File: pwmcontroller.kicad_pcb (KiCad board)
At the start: 2 copper layers, 35.1 x 44.5 mm, 19 parts, among them J1 CONN_01X04, J2 CONN_01X04, U1 WPMIx9200501S, U2 NE555

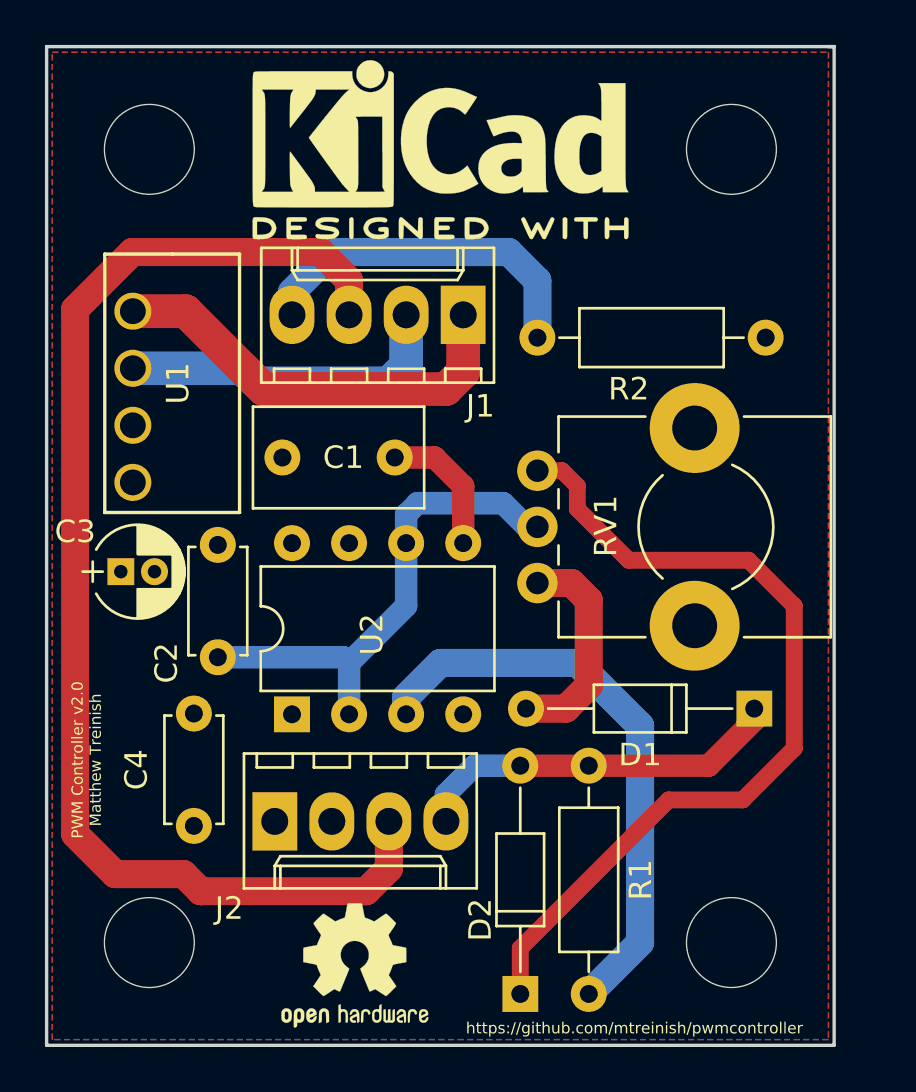
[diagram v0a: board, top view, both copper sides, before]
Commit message: Add fan header labels
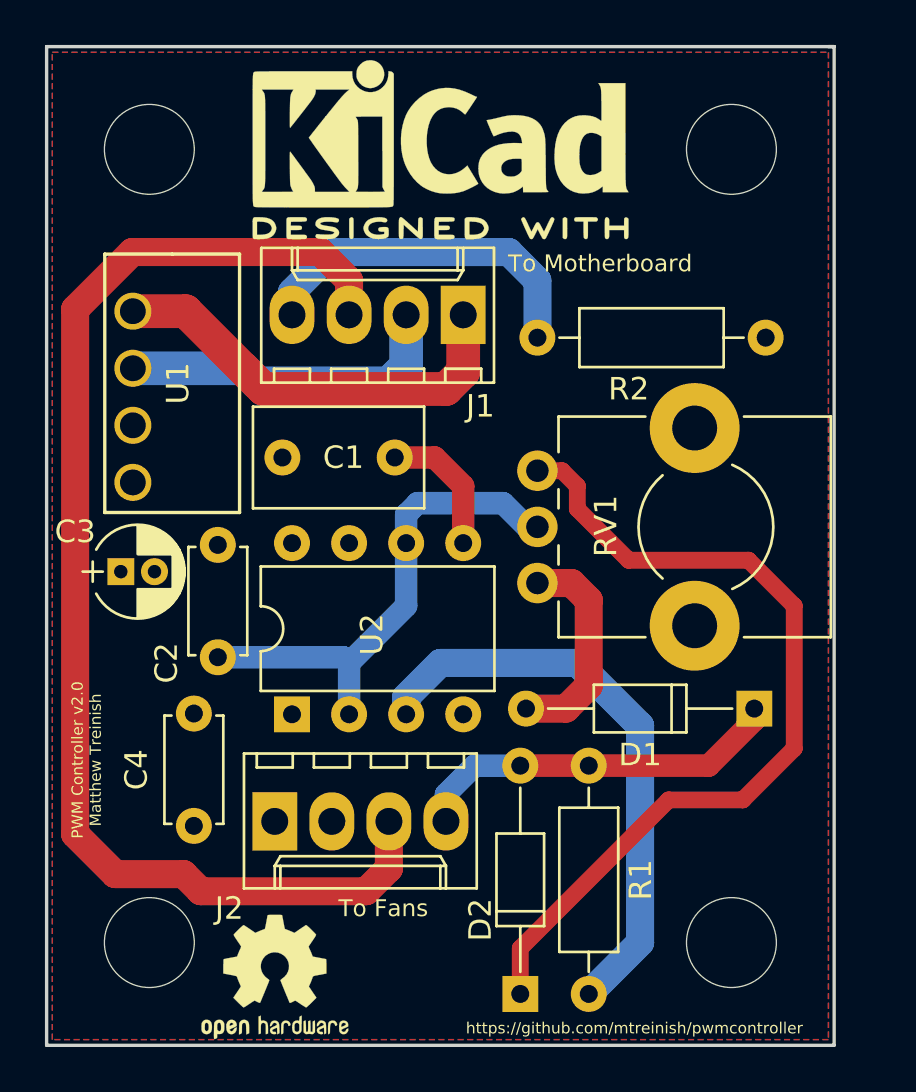
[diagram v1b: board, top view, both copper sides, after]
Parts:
- moved REF*** 3.59 mm to (149.6, 131.3)
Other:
- board text added: "To Fans"
- board text added: "To Motherboard"
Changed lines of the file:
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@@
     (area 139.370999 88.513 174.765001 135.869)
     (thickness 1.6)
-    (drawings 7)
+    (drawings 9)
     (tracks 68)
     (zones 0)
@@
   )
   (module Symbols:OSHW-Logo2_7.3x6mm_SilkScreen (layer F.Cu)
-    (at 153.162 130.81)
+    (at 149.606 131.318)
     (descr "Open Source Hardware Symbol")
     (tags "Logo Symbol OSHW")
@@
     )
   )
+  (gr_text "To Motherboard" (at 164.084 99.568) (layer F.SilkS)
+    (effects (font (size 0.75 0.75) (thickness 0.1875)))
+  )
+  (gr_text "To Fans" (at 154.432 128.27) (layer F.SilkS)
+    (effects (font (size 0.75 0.75) (thickness 0.1875)))
+  )
   (gr_text https://github.com/mtreinish/pwmcontroller (at 165.608 133.604) (layer F.SilkS)

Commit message: Add Schmitt Trigger Output Buffer
This commit adds a schmitt trigger output buffer to clean up the output
signal.
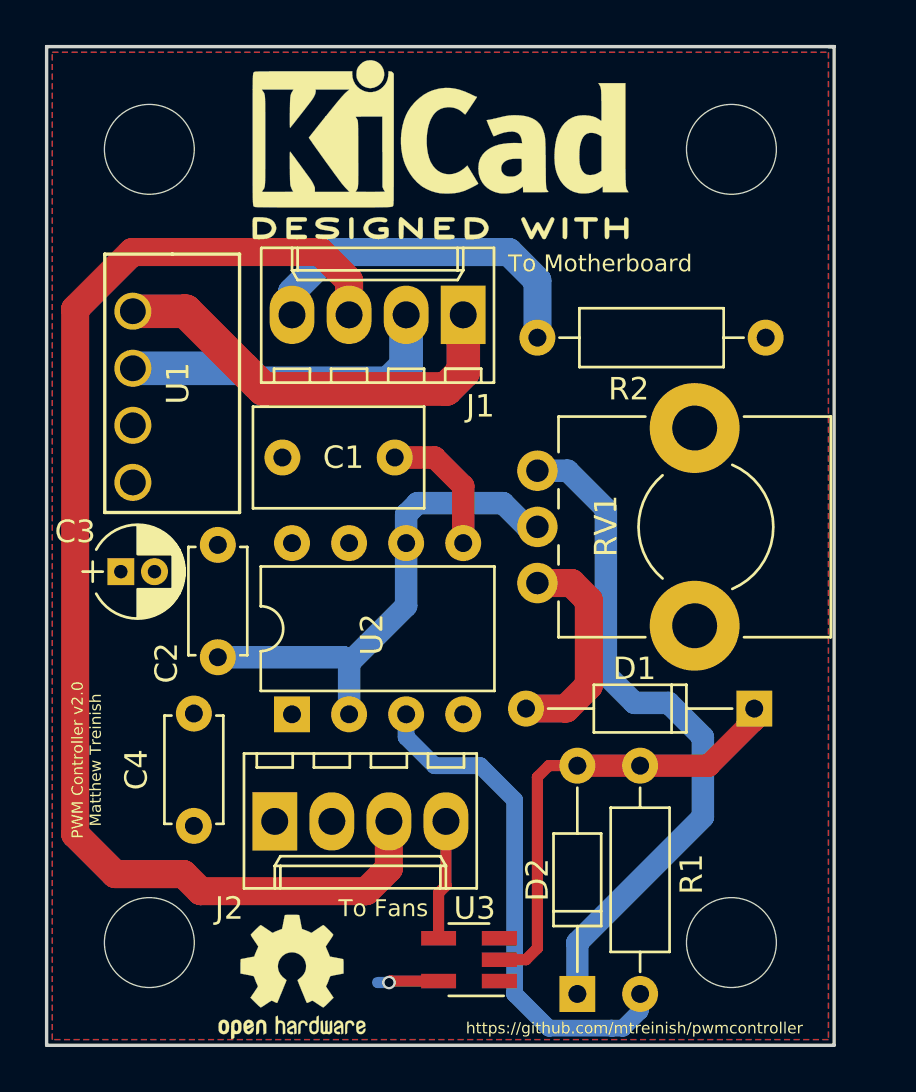
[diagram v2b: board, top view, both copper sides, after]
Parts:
- added U3: 74AHC1G14, TO_SOT_Packages_SMD:SOT-23-5_HandSoldering, F.Cu at (158.2, 130.6)
- moved D2 2.54 mm to (163.1, 132.1)
- moved R1 2.29 mm to (165.9, 121.9)
- moved REF*** 0.76 mm to (150.4, 131.3)
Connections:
- J2 pad 4: /PWM_OUT -> Net-(J2-Pad4)
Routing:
- net Net-(D2-Pad1): track 38.8 -> 30.3 mm
- net Net-(J2-Pad4): track 0.00 -> 5.34 mm
- net /PWM_OUT: track 16.8 -> 21.2 mm
- net Net-(R1-Pad2): track 25.8 -> 22.9 mm
- net VCC: track 0.00 -> 2.74 mm, vias 0 -> 1

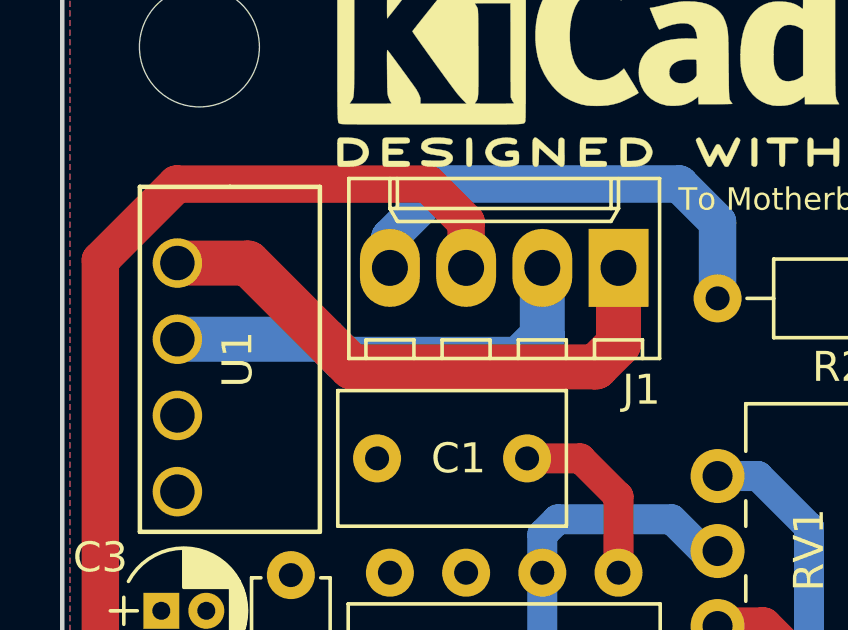
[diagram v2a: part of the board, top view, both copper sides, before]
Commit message: Fix floating output ground
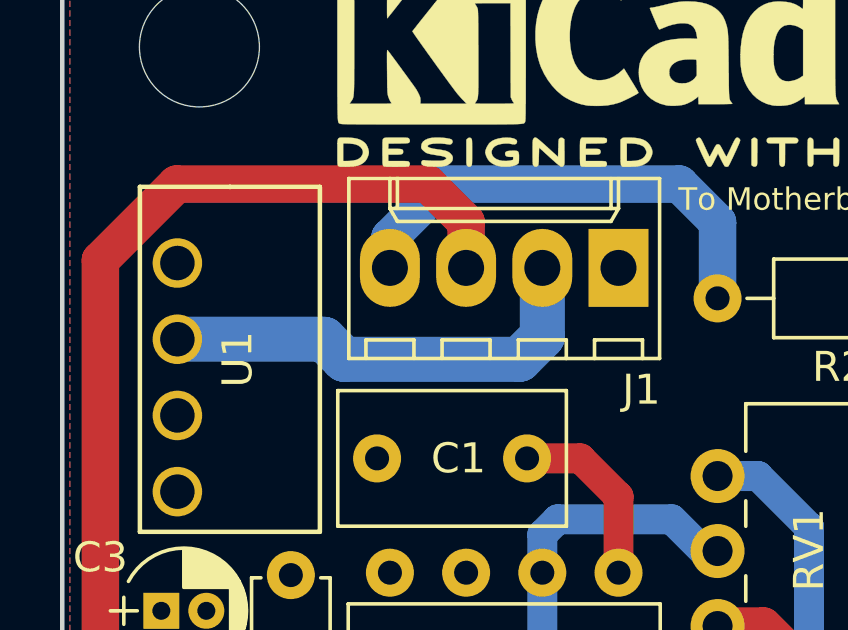
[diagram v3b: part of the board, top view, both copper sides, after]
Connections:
- J1 pad 1: GNDS -> GND
- U1 pad 1: GNDS -> GND
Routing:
- net GNDS: track 19.0 -> 0.00 mm

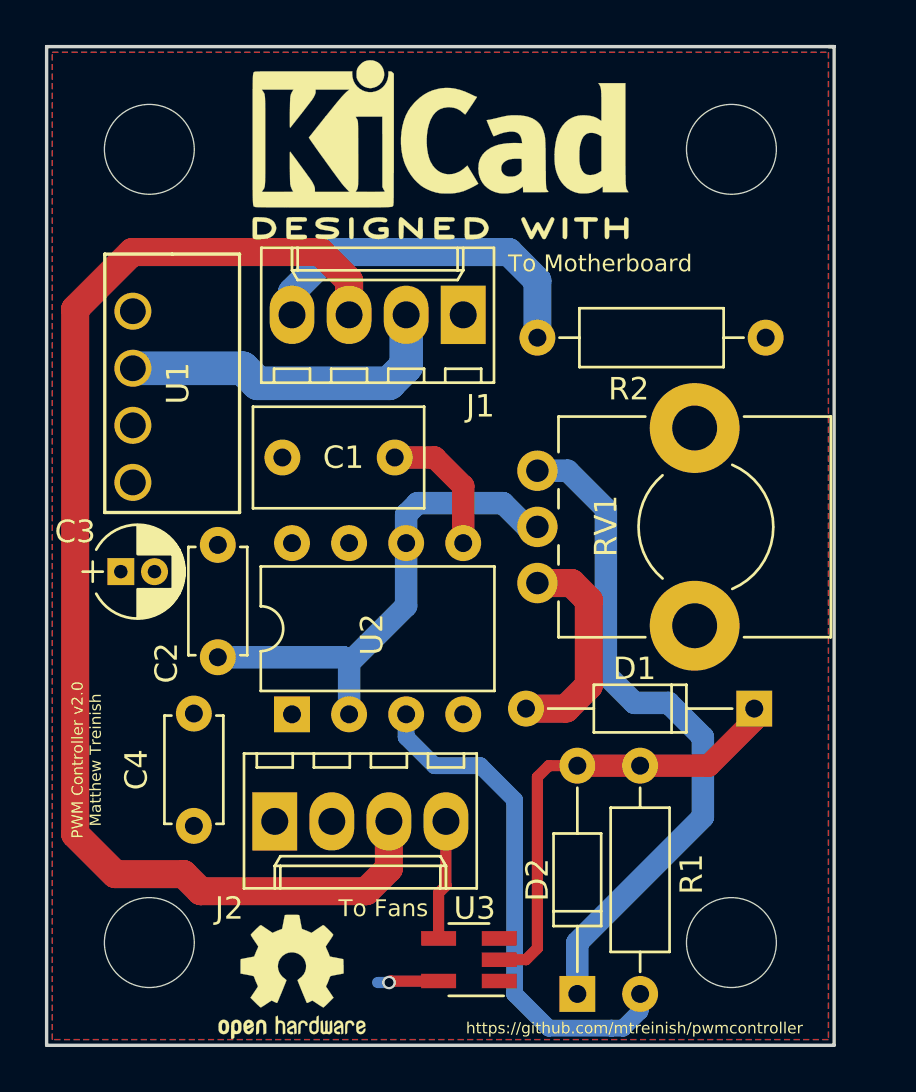
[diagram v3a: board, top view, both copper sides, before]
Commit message: Pivot to revision 3 of the design
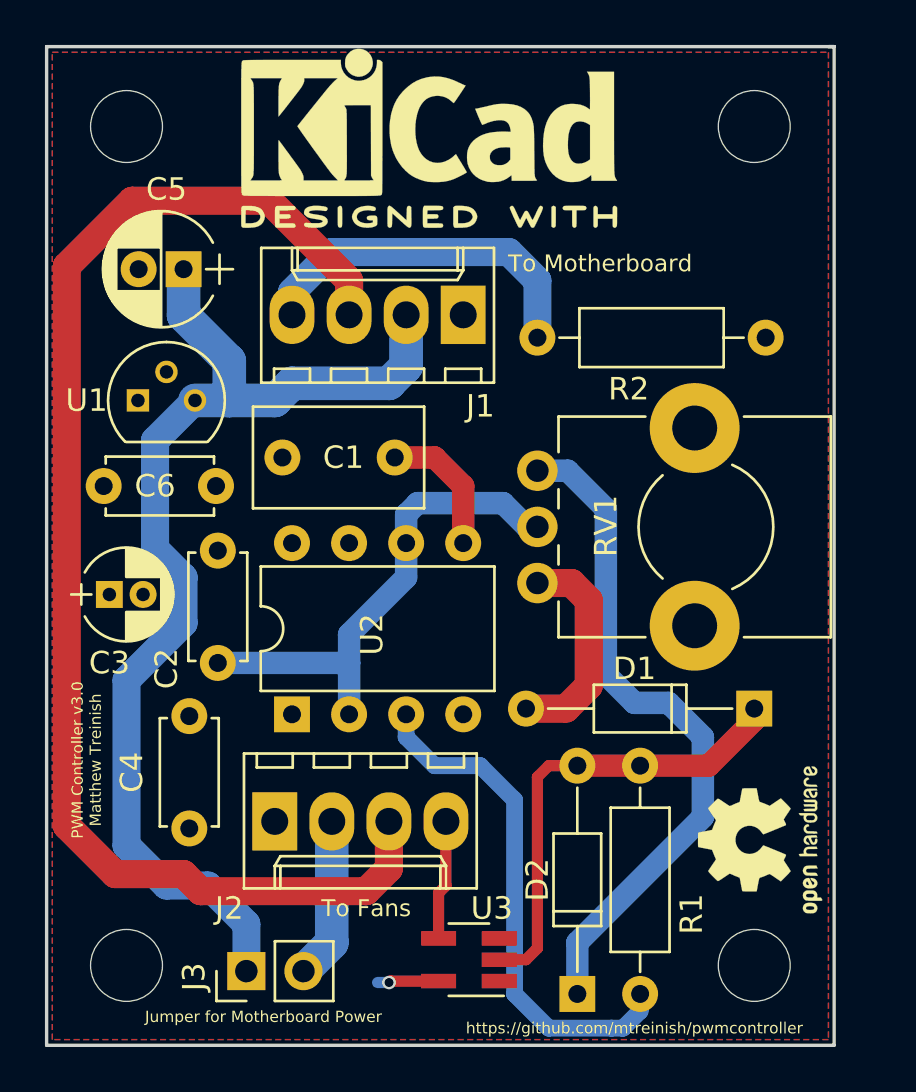
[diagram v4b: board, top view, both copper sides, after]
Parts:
- removed ? (x4): , Mounting_Holes:MountingHole_4mm
- added C5: .33uF, Capacitors_THT:CP_Radial_D5.0mm_P2.00mm, F.Cu at (145.5, 99.8)
- added C6: .1uF, Capacitors_THT:C_Disc_D4.7mm_W2.5mm_P5.00mm, F.Cu at (142.0, 109.5)
- added J3: Conn_01x02_Male, Socket_Strips:Socket_Strip_Straight_1x02_Pitch2.54mm, F.Cu at (148.3, 131.1)
- added REF**: MountingHole_3.2mm_M3, Mounting_Holes:MountingHole_3.2mm_M3, F.Cu at (143.0, 93.5)
- added REF**: MountingHole_3.2mm_M3, Mounting_Holes:MountingHole_3.2mm_M3, F.Cu at (170.9, 93.5)
- added REF**: MountingHole_3.2mm_M3, Mounting_Holes:MountingHole_3.2mm_M3, F.Cu at (170.9, 130.8)
- added REF**: MountingHole_3.2mm_M3, Mounting_Holes:MountingHole_3.2mm_M3, F.Cu at (143.0, 130.8)
- U1: value WPMIx9200501S -> MC78L05_TO92; footprint pwmcontroller:WPMIx9200501S -> TO_SOT_Packages_THT:TO-92_Molded_Narrow
- moved REF*** 21.7 mm to (171.2, 125.2), turned to 90 degrees
- moved U1 1.70 mm to (143.5, 105.7), turned to 0 degrees
- moved C3 1.14 mm to (142.2, 114.3)
- moved REF*** 0.72 mm to (156.5, 94.0)
- moved C2 0.25 mm to (147.1, 117.3)
- moved C4 0.23 mm to (145.8, 124.7)
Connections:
- J2 pad 2: Net-(J2-Pad2) -> /12V_OUT
- U1 pad 1: GND -> VCC
- U1 pad 2: +12V -> GND
- U1 pad 3: GND -> +12V
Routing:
- net +12V: track 15.0 -> 50.0 mm
- net /12V_OUT: track 0.00 -> 7.19 mm
- net /FAN_RPM: track 56.2 -> 59.7 mm
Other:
- board text added: "Jumper for Motherboard Power"
- board text added: "PWM Controller v3.0 Matthew Treinish"
- board text removed: "PWM Controller v2.0 Matthew Treinish"
